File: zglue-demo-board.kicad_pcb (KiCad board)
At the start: 6 copper layers, 56 x 66 mm, 146 parts, among them J1 20021121-00010C4LF, J10 0473460001, J2 DF13A-2P-1.25H, J3 20021121-00010C4LF, J4 2x20_Header_Female, J5 0473460001, J6 556500488, J7 556500488, J8 WE_686115148922, J9 WE_686115148922_FLIPPED, U1 MCP1700T-3302E_TT, U2 NTB0104BQ, U3 NTB0104BQ, U4 NTB0104BQ, U5 93LC56CT-IMC, U6 FT4232HQ, U7 NTB0104BQ, U8 NTB0104BQ, Y1 ASFLMB-12.000MHZ-LC-T

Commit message: Schematic updated after initial bringup
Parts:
- U2, U3, U4: value NTB0104BQ -> NTS0104BQ

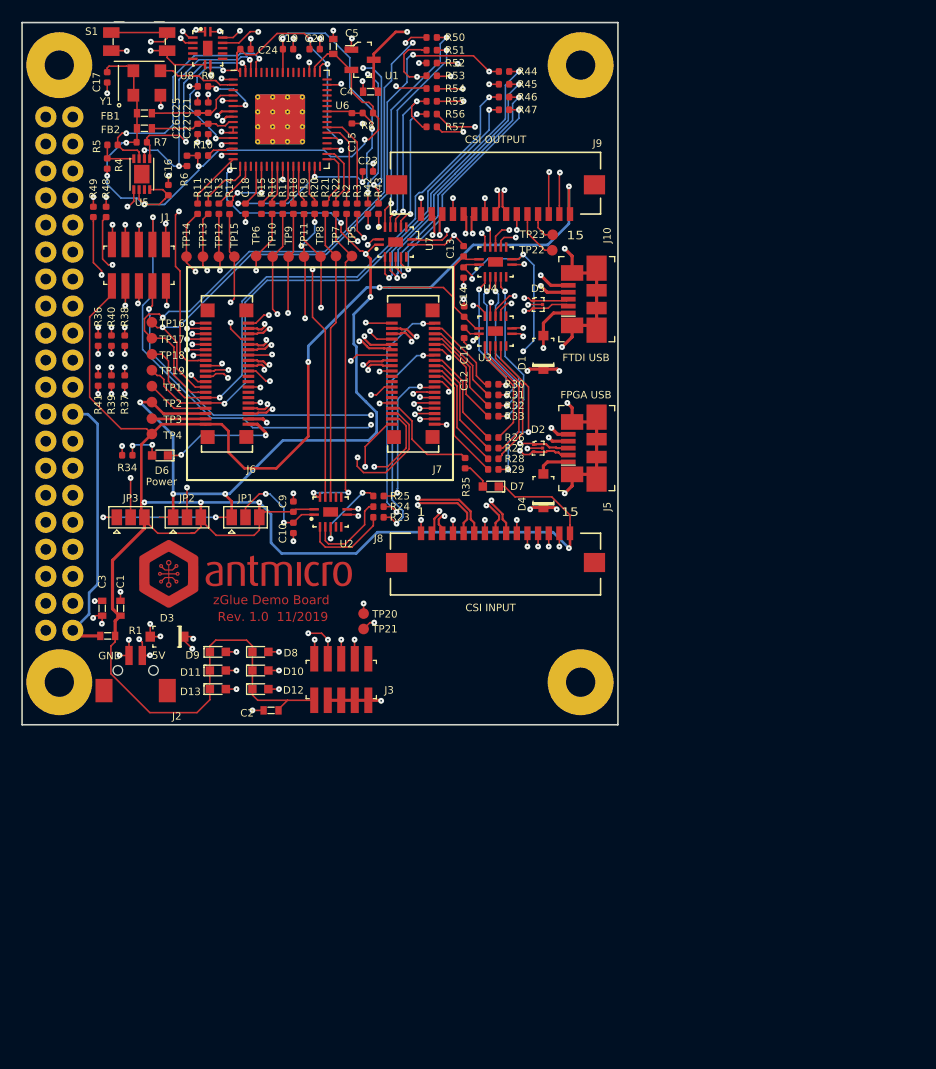
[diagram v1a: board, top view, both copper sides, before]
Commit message: Started revision 1.1, moved components to bottom side
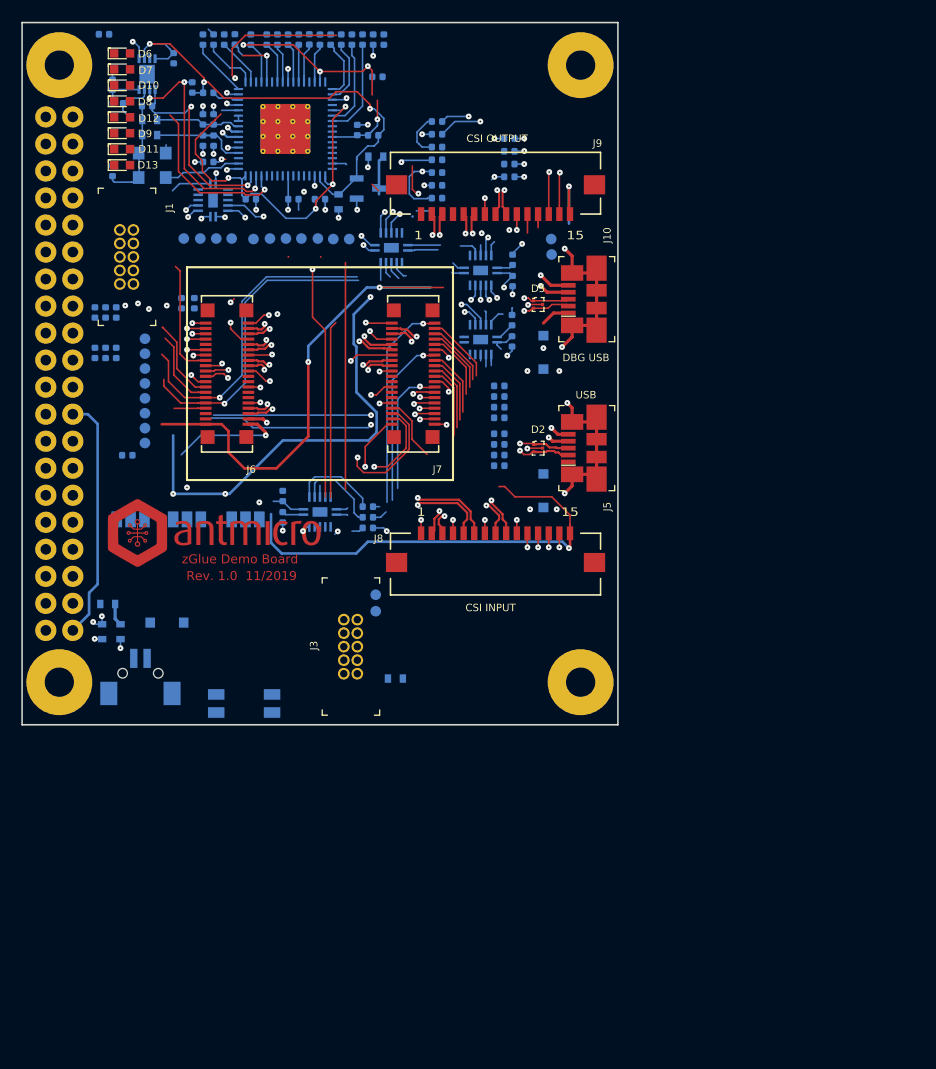
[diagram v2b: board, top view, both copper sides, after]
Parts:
- C1, C10, C11, C12, C13, C14, C15, C16, C17, C18, C19, C2, C20, C21, C22, C23, C24, C25, C26, C3, C4, C5, C9, D1, D3, D4, FB1, FB2, J2, JP1, JP2, JP3, R1, R10, R11, R12, R13, R14, R15, R16, R17, R18, R19, R2, R20, R21, R22, R23, R24, R25, R26, R27, R28, R29, R3, R30, R31, R32, R33, R34, R35, R36, R37, R38, R39, R4, R40, R41, R42, R43, R44, R45, R46, R47, R48, R49, R5, R50, R51, R52, R53, R54, R55, R56, R57, R6, R7, R8, R9, S1, TP1, TP10, TP11, TP12, TP13, TP14, TP15, TP16, TP17, TP18, TP19, TP2, TP20, TP21, TP22, TP23, TP3, TP4, TP5, TP6, TP7, TP8, TP9, U1, U2, U3, U4, U5, U6, U7, U8, Y1: moved to B.Cu
- J1, J3: value 20021121-00010C4LF -> 3220-10-0100-00; footprint antmicro-footprints:PinHeader_2x5_P1.27mm -> antmicro-footprints:PinHeader_2x5_P1.27mm_Drill.7mm
- moved S1 63.0 mm to (20.9, 64.0)
- moved D12 55.3 mm to (9.40, 8.90)
- moved D8 55.1 mm to (9.40, 7.40)
- moved D10 54.8 mm to (9.40, 5.90)
- moved R35 52.7 mm to (7.70, 1.10), turned to 180 degrees
- moved D7 52.3 mm to (9.40, 4.40), turned to 0 degrees
- moved D13 50.1 mm to (9.40, 13.4)
- moved D11 49.8 mm to (9.40, 11.9)
- moved D9 49.6 mm to (9.40, 10.4)
- moved D6 38.0 mm to (9.40, 2.90), turned to 0 degrees
- moved R50 16.3 mm to (39.0, 17.7)
- moved R14 15.9 mm to (20.0, 1.58), turned to 90 degrees
- moved R19 15.9 mm to (27.0, 1.58), turned to 90 degrees
- moved C18 15.9 mm to (21.5, 1.60), turned to 90 degrees
- moved R11 15.9 mm to (17.0, 1.60), turned to 90 degrees
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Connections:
- J4 pad 11: Net-(J4-Pad11) -> /DONE_3V3
- J4 pad 13: Net-(J4-Pad13) -> /CTRL_RST_FLASH_SOC_CS_3V3
- J4 pad 19: Net-(J4-Pad19) -> /E_CTRL_SO_3V3
- J4 pad 21: Net-(J4-Pad21) -> /E_CTRL_SI_3V3
- J4 pad 23: Net-(J4-Pad23) -> /E_CTRL_SCK_3V3
- J4 pad 24: Net-(J4-Pad24) -> /E_CTRL_SS_3V3
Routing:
- net /3V3_SYS: track 284.1 -> 111.9 mm, vias 10 -> 8
- net /VCCIO3: track 74.7 -> 3.93 mm, vias 4 -> 1
- net GND: track 150.6 -> 215.6 mm, vias 82 -> 61
- net /1V8_SYS: track 125.4 -> 61.0 mm, vias 12 -> 7
- net /RPI_SDA: track 80.7 -> 16.4 mm, vias 2 -> 1
- net /RPI_SCL: track 76.3 -> 16.5 mm
- net Net-(J4-Pad10): track 58.9 -> 0.14 mm, vias 1 -> 0
- net /VCCIO2: track 59.6 -> 2.51 mm, vias 3 -> 0
- net /I2C_0_SDA: track 64.4 -> 7.46 mm, vias 3 -> 0
- net (no net): track 0.00 -> 53.2 mm, vias 0 -> 1
- net /I2C_0_SCL: track 58.4 -> 12.2 mm, vias 3 -> 2
- net /E_PROC_SCK_3V3: track 41.9 -> 1.00 mm, vias 2 -> 0
- net /DBG_TX_3V3: track 39.4 -> 1.89 mm, vias 4 -> 1
- net /E_CTRL_SCK_3V3: track 37.7 -> 2.94 mm, vias 2 -> 1
- net /DBG_RX_3V3: track 37.3 -> 4.84 mm, vias 4 -> 2
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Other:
- board text added: "DBG USB"
- board text added: "USB"
- board text removed: "5V"
- board text removed: "FPGA USB"
- board text removed: "FTDI USB"
- board text removed: "GND"
- board text removed: "Power"

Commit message: Routing finished
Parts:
- moved R14 0.34 mm to (20.1, 1.91)
- moved R19 0.34 mm to (27.1, 1.91)
- moved C18 0.34 mm to (21.6, 1.92)
- moved R11 0.34 mm to (17.1, 1.92)
- moved R12 0.34 mm to (18.1, 1.92)
- moved R13 0.34 mm to (19.1, 1.92)
- moved R15 0.34 mm to (23.1, 1.92)
- moved R16 0.34 mm to (24.1, 1.92)
- moved R17 0.34 mm to (25.1, 1.92)
- moved R18 0.34 mm to (26.1, 1.92)
- moved R2 0.34 mm to (31.1, 1.92)
- moved R20 0.34 mm to (28.1, 1.92)
- moved R21 0.34 mm to (29.1, 1.92)
- moved R22 0.34 mm to (30.1, 1.92)
- moved R3 0.34 mm to (32.1, 1.92)
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- renumbered JP1 to VCCIO1, JP2 to VCCIO2, JP3 to VCCIO3
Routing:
- net /3V3_SYS: track 111.9 -> 252.0 mm, vias 8 -> 19
- net /E_CTRL_SO_3V3: track 1.41 -> 85.8 mm, vias 0 -> 8
- net /VCCIO3: track 3.93 -> 84.3 mm, vias 1 -> 4
- net Net-(J4-Pad10): track 0.14 -> 77.8 mm, vias 0 -> 1
- net /E_CTRL_SI_3V3: track 1.78 -> 77.7 mm, vias 0 -> 6
- net /E_CTRL_SS_3V3: track 1.85 -> 74.0 mm, vias 1 -> 6
- net /RPI_SDA: track 16.4 -> 85.6 mm, vias 1 -> 2
- net /RPI_SCL: track 16.5 -> 83.9 mm, vias 1 -> 2
- net /E_CTRL_SCK_3V3: track 2.94 -> 69.9 mm, vias 1 -> 5
- net /CTRL_RST_FLASH_SOC_CS_3V3: track 22.9 -> 88.2 mm, vias 2 -> 6
- net /DONE_3V3: track 16.7 -> 80.8 mm, vias 0 -> 5
- net /VCCIO2: track 2.51 -> 66.2 mm, vias 0 -> 4
- net /1V8_SYS: track 61.0 -> 123.1 mm, vias 7 -> 9
- net /E_PROC_SCK_3V3: track 1.00 -> 56.4 mm, vias 0 -> 4
- net /CTRL_OUT: track 6.12 -> 61.1 mm, vias 0 -> 3
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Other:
- board text added: "5V"
- board text added: "GND"
- board text added: "Rev. 1.1 11/2019"
- board text removed: "Rev. 1.0 11/2019"

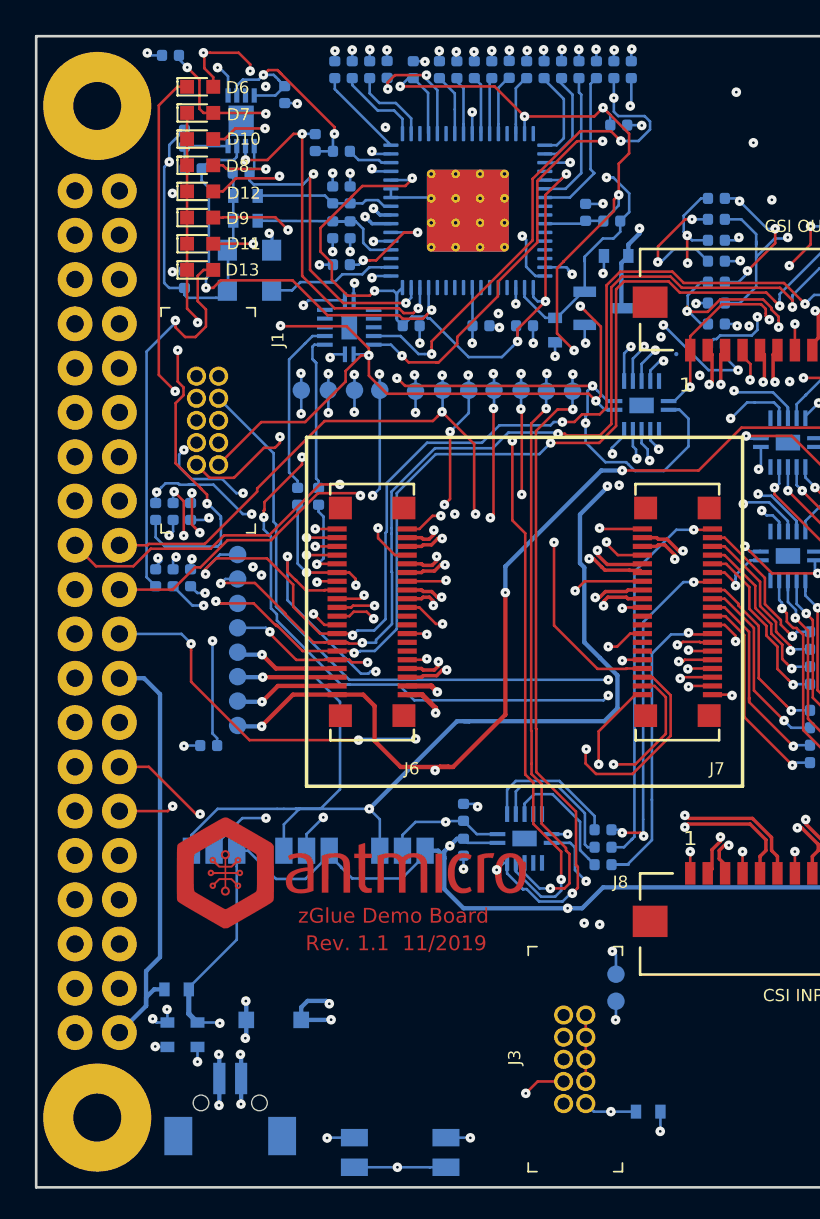
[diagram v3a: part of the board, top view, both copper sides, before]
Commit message: Tied SPI signals for programming second FPGA from RPi
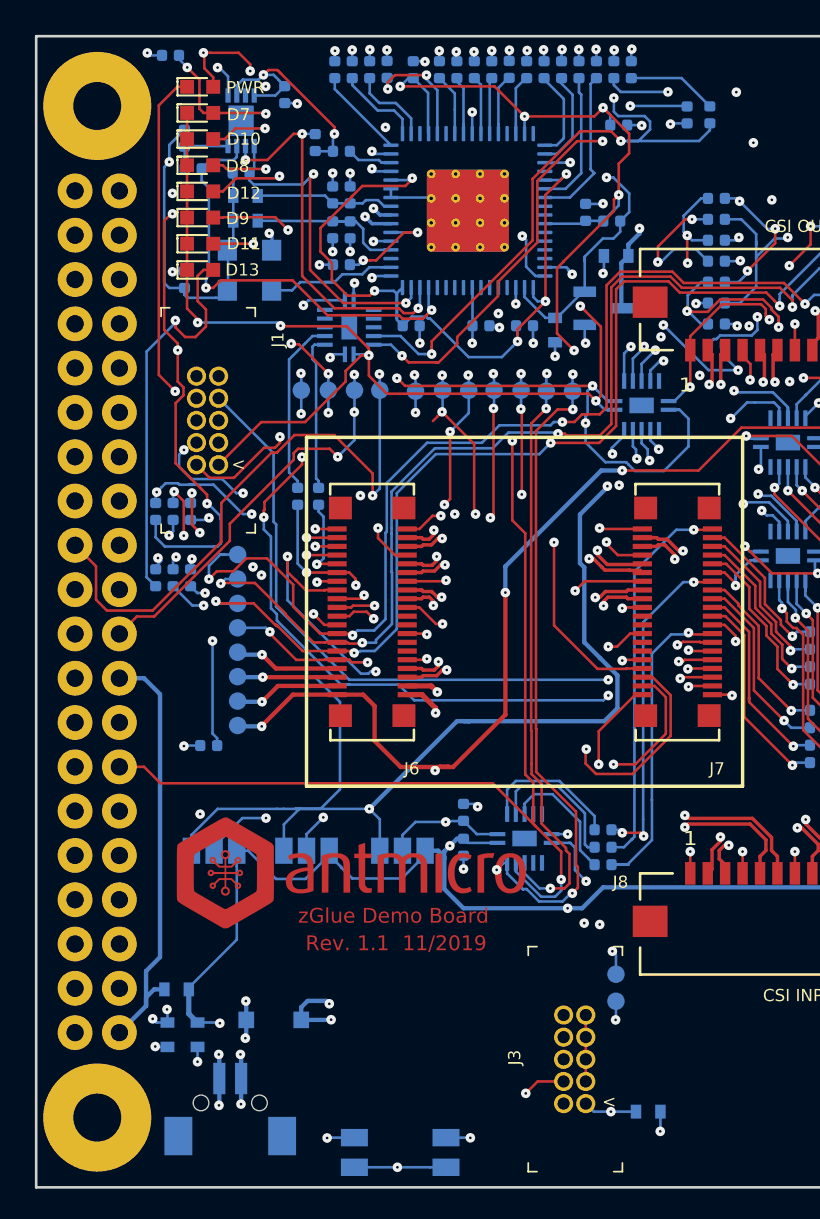
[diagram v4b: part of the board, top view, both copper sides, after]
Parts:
- added R58: R_0R_0402, antmicro-footprints:0402-res, B.Cu at (37.3, 4.51)
- added R59: R_0R_0402, antmicro-footprints:0402-res, B.Cu at (38.6, 4.51)
- renumbered VCCIO1 to JP1, VCCIO2 to JP2, VCCIO3 to JP3, D6 to PWR
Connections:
- J4 pad 11: /DONE_3V3 -> Net-(J4-Pad11)
- J4 pad 13: /CTRL_RST_FLASH_SOC_CS_3V3 -> /E_PROC_RST_3V3
- J4 pad 19: /E_CTRL_SO_3V3 -> /E_PROC_SI_3V3
- J4 pad 21: /E_CTRL_SI_3V3 -> /E_PROC_SO_3V3
- J4 pad 23: /E_CTRL_SCK_3V3 -> /E_PROC_SCK_3V3
- J4 pad 24: /E_CTRL_SS_3V3 -> /E_PROC_SS_3V3
- R42 pad 2: /DBG_RX_3V3 -> /RPI_DBG_RX_3V3
- R43 pad 2: /DBG_TX_3V3 -> /RPI_DBG_TX_3V3
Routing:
- net /E_CTRL_SO_3V3: track 85.8 -> 50.2 mm, vias 8 -> 5
- net /E_PROC_SO_3V3: track 60.8 -> 92.8 mm, vias 5 -> 6
- net /E_CTRL_SS_3V3: track 74.0 -> 46.2 mm, vias 6 -> 5
- net /E_PROC_SS_3V3: track 60.0 -> 87.4 mm
- net /DONE_3V3: track 80.8 -> 53.8 mm, vias 5 -> 4
- net /E_PROC_RST_3V3: track 59.7 -> 85.0 mm
- net /E_PROC_SCK_3V3: track 56.4 -> 79.8 mm
- net /E_CTRL_SCK_3V3: track 69.9 -> 48.9 mm
- net /E_PROC_SI_3V3: track 57.2 -> 78.1 mm, vias 5 -> 6
- net /E_CTRL_SI_3V3: track 77.7 -> 61.8 mm
- net /RPI_DBG_RX_3V3: track 0.00 -> 6.54 mm, vias 0 -> 2
- net /CTRL_RST_FLASH_SOC_CS_3V3: track 88.2 -> 82.6 mm
- net /RPI_DBG_TX_3V3: track 0.00 -> 5.45 mm
- net /DBG_RX_3V3: track 33.5 -> 37.8 mm
- net /DBG_TX_3V3: track 30.7 -> 32.5 mm
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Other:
- board text added: "<"
- board text added: "JTAG"
- board text added: "QSPI FLASH"

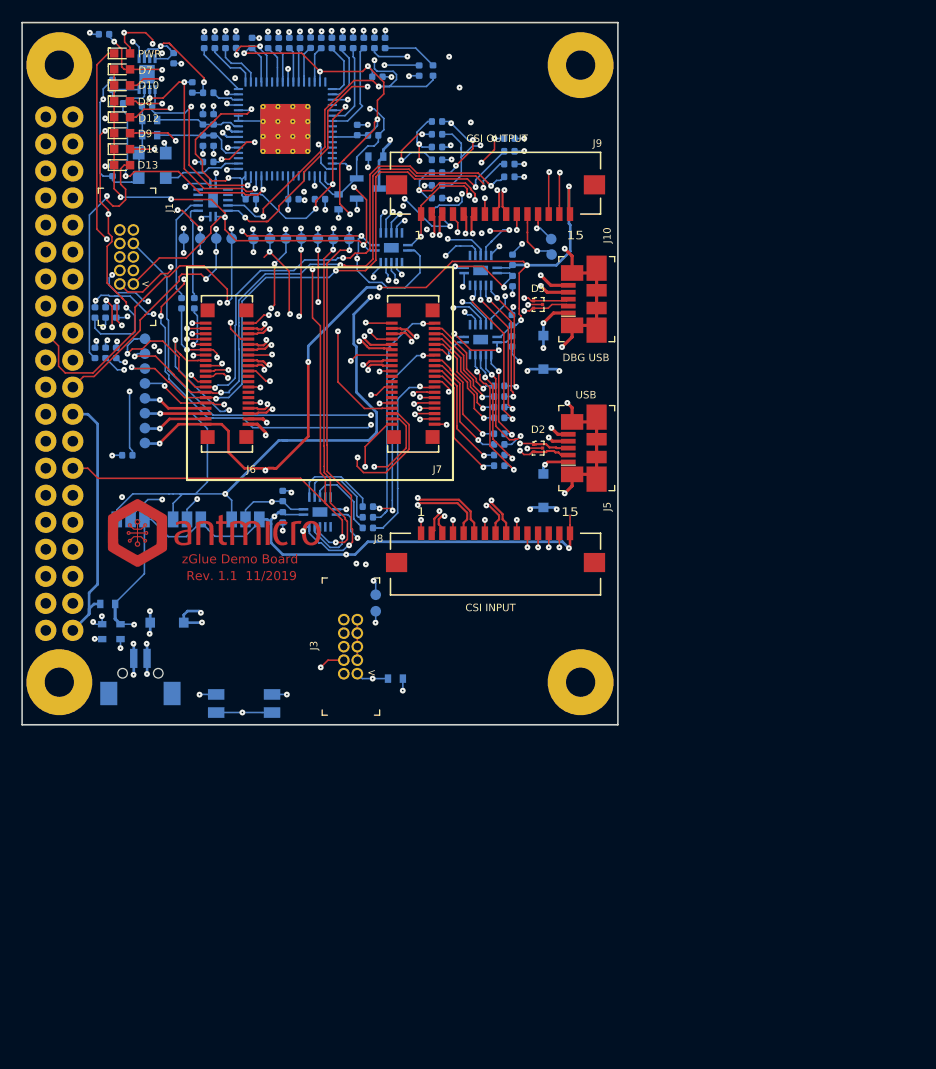
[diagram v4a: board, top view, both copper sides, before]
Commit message: PCB cleanup, updated layout
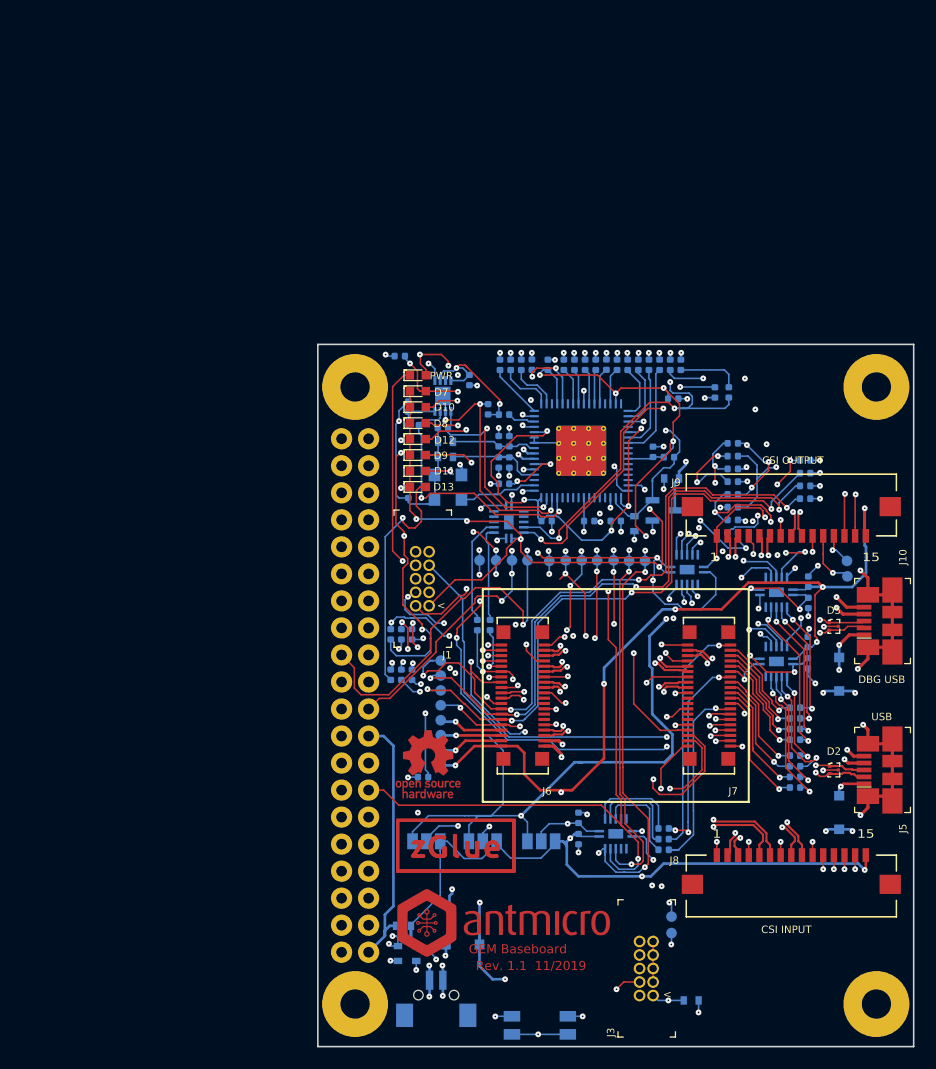
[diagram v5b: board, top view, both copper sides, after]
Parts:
- added N2: zglue_logo_500mil, antmicro-footprints:zglue-logo-10000dpi, F.Cu at (40.8, 77.4)
- added N2: zglue_logo, antmicro-footprints:zglue-logo, F.Cu at (40.8, 77.4)
- added N3: oshw_logo, antmicro-footprints:oshw-logo, F.Cu at (38.2, 69.7)
- moved N1 45.6 mm to (45.3, 84.8)
- moved C13 41.1 mm to (73.9, 52.5)
- moved C14 41.1 mm to (73.9, 54.5)
- moved D3 41.1 mm to (41.4, 86.7)
- moved R1 41.1 mm to (35.9, 84.9)
- moved R26 41.1 mm to (72.7, 68.9)
- moved R27 41.1 mm to (72.7, 69.9)
- moved R28 41.1 mm to (72.7, 70.9)
- moved R29 41.1 mm to (72.7, 71.9)
- moved R30 41.1 mm to (72.7, 64.4)
- moved R31 41.1 mm to (72.7, 65.4)
- moved R32 41.1 mm to (72.7, 66.4)
- moved R33 41.1 mm to (72.7, 67.4)
- moved TP19 41.1 mm to (39.4, 64.1)
- moved TP2 41.1 mm to (39.4, 66.9)
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- renumbered JP1 to VCCIO1, JP2 to VCCIO2, JP3 to VCCIO3
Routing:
- net /VUSB: track 64.3 -> 69.7 mm
- net /5V0_IN: track 5.81 -> 10.2 mm
- net /3V3_SYS: track 252.0 -> 250.6 mm
- net Net-(R25-Pad2): track 7.46 -> 8.70 mm
- net Net-(R23-Pad2): track 7.94 -> 8.74 mm
- net /RPI_DBG_TX_3V3: track 5.45 -> 6.16 mm
- net Net-(R24-Pad2): track 8.44 -> 9.14 mm
- net /CTRL_RST_FLASH_SOC_CS_3V3: track 82.6 -> 83.3 mm
- net GND: track 182.9 -> 183.5 mm
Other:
- board text added: "GEM Baseboard"
- board text removed: "zGlue Demo Board"
